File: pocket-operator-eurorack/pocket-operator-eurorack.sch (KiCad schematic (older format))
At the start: 28 parts, among them J1 Conn_02x05_Odd_Even, J10 Conn_01x01, J11 Conn_01x01, J12 Conn_01x01, J13 Conn_01x01, J2 Conn_02x04_Odd_Even, J6 Conn_01x01, J7 Conn_01x01, J8 Conn_01x01, J9 Conn_01x01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

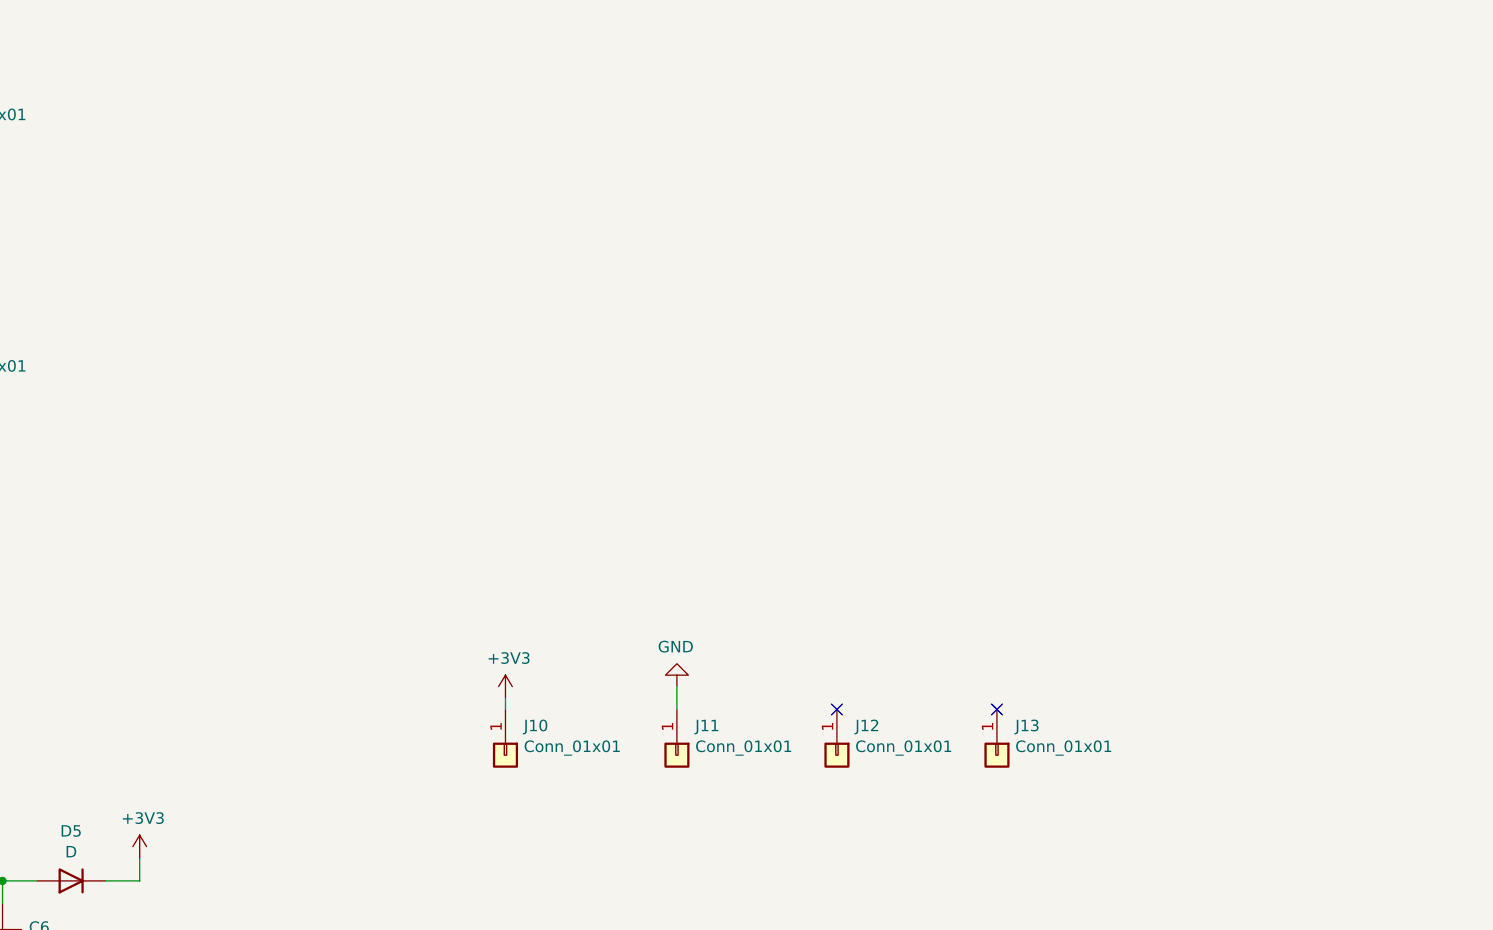
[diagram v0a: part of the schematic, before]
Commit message: connector board added, main board changed to fit connectors correctly
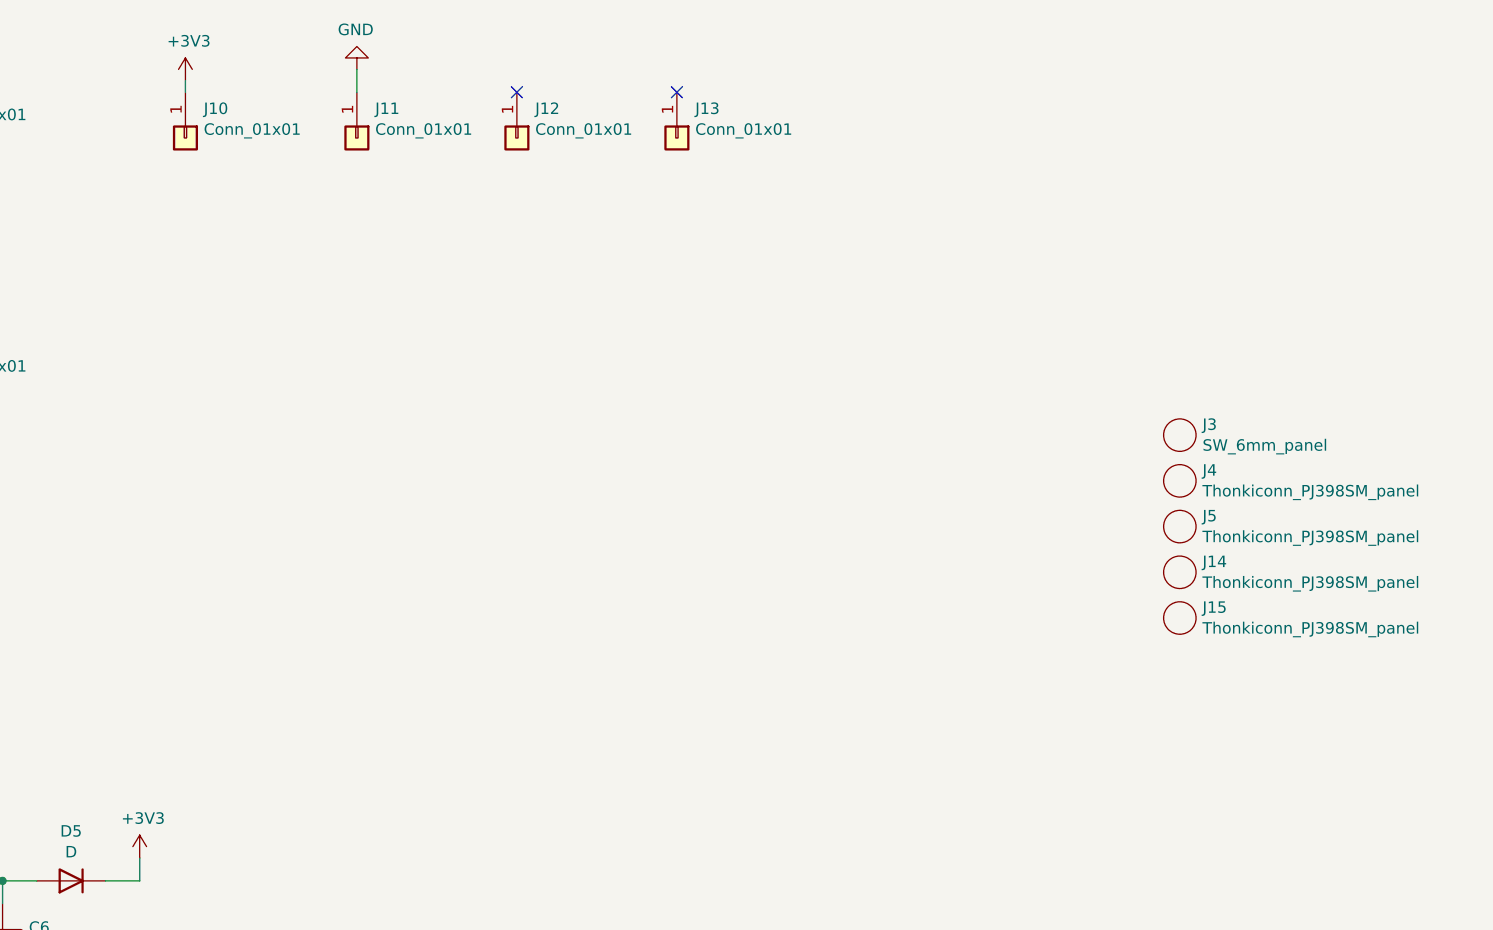
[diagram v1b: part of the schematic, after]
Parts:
- added J14, J15, J4, J5: Thonkiconn_PJ398SM_panel, mylibs:Thonkiconn_PJ398SM_panel, symbol mylibs:Thonkiconn_PJ398SM_panel
- added J3: SW_6mm_panel, mylibs:SW_6mm_panel, symbol mylibs:SW_6mm_panel
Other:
- moved on the sheet: J10, J11, J12, J13
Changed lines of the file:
@@
 L Connector_Generic:Conn_01x01 J10
 U 1 1 61F33A38
-P 6650 4100
-F 0 "J10" V 6522 4180 50  0000 L CNN
-F 1 "Conn_01x01" V 6613 4180 50  0000 L CNN
-F 2 "pocket-operator-eurorack_lib:7mm_solder_pad" H 6650 4100 50  0001 C CNN
-F 3 "~" H 6650 4100 50  0001 C CNN
-	1    6650 4100
+P 5250 1400
+F 0 "J10" V 5122 1480 50  0000 L CNN
+F 1 "Conn_01x01" V 5213 1480 50  0000 L CNN
+F 2 "pocket-operator-eurorack_lib:7mm_solder_pad" H 5250 1400 50  0001 C CNN
+F 3 "~" H 5250 1400 50  0001 C CNN
+	1    5250 1400
 	0    1    1    0
 $EndComp
@@
 L power:+3V3 #PWR023
 U 1 1 61F34398
-P 6650 3850
-F 0 "#PWR023" H 6650 3700 50  0001 C CNN
-F 1 "+3V3" H 6665 4023 50  0000 C CNN
-F 2 "" H 6650 3850 50  0001 C CNN
-F 3 "" H 6650 3850 50  0001 C CNN
-	1    6650 3850
-	1    0    0    -1
-$EndComp
-Wire Wire Line
-	6650 3850 6650 3900
+P 5250 1150
+F 0 "#PWR023" H 5250 1000 50  0001 C CNN
+F 1 "+3V3" H 5265 1323 50  0000 C CNN
+F 2 "" H 5250 1150 50  0001 C CNN
+F 3 "" H 5250 1150 50  0001 C CNN
+	1    5250 1150
+	1    0    0    -1
+$EndComp
+Wire Wire Line
+	5250 1150 5250 1200
 $Comp
 L Connector_Generic:Conn_01x01 J11
 U 1 1 61F3687B
-P 7400 4100
-F 0 "J11" V 7272 4180 50  0000 L CNN
-F 1 "Conn_01x01" V 7363 4180 50  0000 L CNN
-F 2 "pocket-operator-eurorack_lib:7mm_solder_pad" H 7400 4100 50  0001 C CNN
-F 3 "~" H 7400 4100 50  0001 C CNN
-	1    7400 4100
+P 6000 1400
+F 0 "J11" V 5872 1480 50  0000 L CNN
+F 1 "Conn_01x01" V 5963 1480 50  0000 L CNN
+F 2 "pocket-operator-eurorack_lib:7mm_solder_pad" H 6000 1400 50  0001 C CNN
+F 3 "~" H 6000 1400 50  0001 C CNN
+	1    6000 1400
 	0    1    1    0
 $EndComp
@@
 L power:GND #PWR024
 U 1 1 61F37DCA
-P 7400 3800
-F 0 "#PWR024" H 7400 3550 50  0001 C CNN
-F 1 "GND" H 7405 3627 50  0000 C CNN
-F 2 "" H 7400 3800 50  0001 C CNN
-F 3 "" H 7400 3800 50  0001 C CNN
-	1    7400 3800
+P 6000 1100
+F 0 "#PWR024" H 6000 850 50  0001 C CNN
+F 1 "GND" H 6005 927 50  0000 C CNN
+F 2 "" H 6000 1100 50  0001 C CNN
+F 3 "" H 6000 1100 50  0001 C CNN
+	1    6000 1100
 	-1   0    0    1
 $EndComp
 Wire Wire Line
-	7400 3800 7400 3900
+	6000 1100 6000 1200
 $Comp
 L Connector_Generic:Conn_01x01 J12
 U 1 1 61F38DC9
-P 8100 4100
-F 0 "J12" V 7972 4180 50  0000 L CNN
-F 1 "Conn_01x01" V 8063 4180 50  0000 L CNN
-F 2 "pocket-operator-eurorack_lib:7mm_solder_pad" H 8100 4100 50  0001 C CNN
-F 3 "~" H 8100 4100 50  0001 C CNN
-	1    8100 4100
+P 6700 1400
+F 0 "J12" V 6572 1480 50  0000 L CNN
+F 1 "Conn_01x01" V 6663 1480 50  0000 L CNN
+F 2 "pocket-operator-eurorack_lib:7mm_solder_pad" H 6700 1400 50  0001 C CNN
+F 3 "~" H 6700 1400 50  0001 C CNN
+	1    6700 1400
 	0    1    1    0
 $EndComp
@@
 L Connector_Generic:Conn_01x01 J13
 U 1 1 61F392BF
-P 8800 4100
-F 0 "J13" V 8672 4180 50  0000 L CNN
-F 1 "Conn_01x01" V 8763 4180 50  0000 L CNN
-F 2 "pocket-operator-eurorack_lib:7mm_solder_pad" H 8800 4100 50  0001 C CNN
-F 3 "~" H 8800 4100 50  0001 C CNN
-	1    8800 4100
-	0    1    1    0
-$EndComp
-NoConn ~ 8100 3900
-NoConn ~ 8800 3900
+P 7400 1400
+F 0 "J13" V 7272 1480 50  0000 L CNN
+F 1 "Conn_01x01" V 7363 1480 50  0000 L CNN
+F 2 "pocket-operator-eurorack_lib:7mm_solder_pad" H 7400 1400 50  0001 C CNN
+F 3 "~" H 7400 1400 50  0001 C CNN
+	1    7400 1400
+	0    1    1    0
+$EndComp
+NoConn ~ 6700 1200
+NoConn ~ 7400 1200
 $Comp
 L Connector_Generic:Conn_01x01 J8
@@
 Wire Wire Line
 	1950 2900 2400 2900
+$Comp
+L mylibs:SW_6mm_panel J3
+U 1 1 61D46000
+P 9600 2700
+F 0 "J3" H 9699 2746 50  0000 L CNN
+F 1 "SW_6mm_panel" H 9699 2655 50  0000 L CNN
+F 2 "mylibs:SW_6mm_panel" H 9600 2700 50  0001 C CNN
+F 3 "" H 9600 2700 50  0001 C CNN
+	1    9600 2700
+	1    0    0    -1
+$EndComp
+$Comp
+L mylibs:Thonkiconn_PJ398SM_panel J4
+U 1 1 61D46BDF
+P 9600 2900
+F 0 "J4" H 9699 2946 50  0000 L CNN
+F 1 "Thonkiconn_PJ398SM_panel" H 9699 2855 50  0000 L CNN
+F 2 "mylibs:Thonkiconn_PJ398SM_panel" H 9600 2900 50  0001 C CNN
+F 3 "" H 9600 2900 50  0001 C CNN
+	1    9600 2900
+	1    0    0    -1
+$EndComp
+$Comp
+L mylibs:Thonkiconn_PJ398SM_panel J5
+U 1 1 61D46E7A
+P 9600 3100
+F 0 "J5" H 9699 3146 50  0000 L CNN
+F 1 "Thonkiconn_PJ398SM_panel" H 9699 3055 50  0000 L CNN
+F 2 "mylibs:Thonkiconn_PJ398SM_panel" H 9600 3100 50  0001 C CNN
+F 3 "" H 9600 3100 50  0001 C CNN
+	1    9600 3100
+	1    0    0    -1
+$EndComp
+$Comp
+L mylibs:Thonkiconn_PJ398SM_panel J14
+U 1 1 61D47146
+P 9600 3300
+F 0 "J14" H 9699 3346 50  0000 L CNN
+F 1 "Thonkiconn_PJ398SM_panel" H 9699 3255 50  0000 L CNN
+F 2 "mylibs:Thonkiconn_PJ398SM_panel" H 9600 3300 50  0001 C CNN
+F 3 "" H 9600 3300 50  0001 C CNN
+	1    9600 3300
+	1    0    0    -1
+$EndComp
+$Comp
+L mylibs:Thonkiconn_PJ398SM_panel J15
+U 1 1 61D473EA
+P 9600 3500
+F 0 "J15" H 9699 3546 50  0000 L CNN
+F 1 "Thonkiconn_PJ398SM_panel" H 9699 3455 50  0000 L CNN
+F 2 "mylibs:Thonkiconn_PJ398SM_panel" H 9600 3500 50  0001 C CNN
+F 3 "" H 9600 3500 50  0001 C CNN
+	1    9600 3500
+	1    0    0    -1
+$EndComp
 $EndSCHEMATC
